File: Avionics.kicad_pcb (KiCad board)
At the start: 4 copper layers, 321.1 x 96.2 mm, 81 parts, among them J1 54-00175, U1 OEM719, U2 TCAN1051VDRBRQ1, U3 INA260AIPWR, U4 TCAN1051VDRBRQ1, U5 INA260AIPWR, U6 TPS543320RPYR

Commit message: OBC: Continue PCB lauout
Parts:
- removed the C3 at (85.9, 65.8)
- removed the C4 at (87.9, 65.8)
- removed the C5 at (83.6, 58.2)
- removed the C6 at (83.6, 60.2)
- removed H1 (x2), H2 (x2): Conn_02x26_Odd_Even, VST104_footprints:ESQ-126-39-x-D
- removed the JP1 at (77.2, 69.9)
- removed the JP2 at (73.8, 69.9)
- removed JP3, JP4: ~, Jumper:SolderJumper-2_P1.3mm_Open_RoundedPad1.0x1.5mm
- removed the MH1 at (181.9, 40.2)
- removed the MH1 at (296.7, 39.9)
- removed the MH2 at (370.3, 39.9)
- removed the MH2 at (255.5, 40.2)
- removed the MH3 at (372.9, 125.7)
- removed the MH3 at (258.1, 125.9)
- removed the MH4 at (292.9, 125.7)
- removed the MH4 at (178.1, 125.9)
- removed the U2 at (87.2, 61.1)
- removed the U4 at (75.4, 75.3)
- added H1COMM1: Conn_02x26_Odd_Even, ESQ-126-39-G-D:SAMTEC_ESQ-126-39-G-D, F.Cu at (186.9, 47.9)
- added H1EPS1: Conn_02x26_Odd_Even, ESQ-126-39-G-D:SAMTEC_ESQ-126-39-G-D, F.Cu at (301.4, 43.1)
- added H2COMM1: Conn_02x26_Odd_Even, ESQ-126-39-G-D:SAMTEC_ESQ-126-39-G-D, F.Cu at (186.9, 42.8)
- added H2EPS1: Conn_02x26_Odd_Even, ESQ-126-39-G-D:SAMTEC_ESQ-126-39-G-D, F.Cu at (301.4, 48.2)
- added J1: SQT-110-01-L-D, SQT-110-01-L-D:SAMTEC_SQT-110-01-L-D, F.Cu at (113.3, 52.1)
- added R7: 1k, Resistor_SMD:R_0805_2012Metric, B.Cu at (62.9, 110.2)
- added R8: 1k, Resistor_SMD:R_0805_2012Metric, B.Cu at (62.9, 113.5)
- added U3: TCAN1046AVDYYRQ1, TCAN1046AV:SOT23_DYY_TEX, B.Cu at (78.1, 64.5)
- H1OBC1: renamed from H1; footprint VST104_footprints:ESQ-126-39-x-D -> ESQ-126-39-G-D:SAMTEC_ESQ-126-39-G-D
- H2OBC1: renamed from H2; footprint VST104_footprints:ESQ-126-39-x-D -> ESQ-126-39-G-D:SAMTEC_ESQ-126-39-G-D
- moved MH5 270.7 mm to (181.9, 40.2)
- moved MH8 249.3 mm to (178.1, 126.0)
- moved MH6 220.4 mm to (255.5, 40.2)
- moved MH9 189.6 mm to (296.3, 40.6)
- moved MH10 178.6 mm to (370.0, 40.6)
- moved MH7 169.8 mm to (258.1, 126.0)
- moved MH12 153.0 mm to (292.5, 126.3)
- moved MH11 90.8 mm to (372.5, 126.3)
- moved C8 51.1 mm to (127.6, 69.0), turned to 180 degrees
- moved U4 50.9 mm to (122.3, 70.9)
- moved R13 18.5 mm to (120.7, 83.6)
- moved C10 18.5 mm to (127.3, 85.3)
- moved C11 18.5 mm to (129.3, 85.3)
- moved C15 18.5 mm to (118.8, 81.0)
- moved C16 18.5 mm to (109.6, 88.6)
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- renumbered C14 to C10, C15 to C11, C16 to C12, C17 to C13, C18 to C14, C19 to C15, C20 to C16, C21 to C17, C22 to C18, C7 to C3, C8 to C4, C9 to C5, C10 to C6, C11 to C7, C12 to C8, C13 to C9, J1 to J2, JP5 to JP1, JP6 to JP2, R8 to R10, R9 to R11, R10 to R12, R11 to R13, R12 to R14, R13 to R15, R14 to R16, R15 to R17, R7 to R9, U3 to U2, U5 to U4, U6 to U5
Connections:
- C16 pad 1: /OBC/TPS543320/VOUT -> /OBC/+5V_OEM719B
- C17 pad 1: /OBC/TPS543320/VOUT -> /OBC/+5V_OEM719B
- C18 pad 1: /OBC/TPS543320/VOUT -> /OBC/+5V_OEM719B
- C4 pad 1: +5V_CM4 -> +3V3
- C5 pad 1: +5V_CM4 -> +3V3
- C6 pad 1: +3V3 -> +5V_CM4
- C7 pad 1: +3V3 -> +5V_CM4
- J2 pad 2: Net-(U1-RXD1) -> /OBC/GNSS_RXD1
- J2 pad 3: Net-(U1-TXD1) -> /OBC/GNSS_TXD1
- JP1 pad 2: Net-(JP5-B) -> Net-(JP1-B)
- JP2 pad 1: Net-(JP6-A) -> Net-(JP2-A)
- L1 pad 2: /OBC/TPS543320/VOUT -> /OBC/+5V_OEM719B
- Module1 pad 34: /OBC/GNSS_RXD -> /OBC/GNSS_RXD2
- Module1 pad 54: /OBC/GNSS_TXD -> /OBC/GNSS_TXD2
- Module1 pad 89: Net-(JP5-B) -> Net-(Module1A-WiFi_nDisable)
- Module1 pad 91: Net-(JP6-A) -> Net-(Module1A-BT_nDisable)
- Module1 pad SH1: GND -> (no net)
- Module1 pad SH2: GND -> (no net)
- Module1 pad SH3: GND -> (no net)
- Module1 pad SH4: GND -> (no net)
- R1 pad 1: Net-(JP1-A) -> /OBC/CAN_A_H
- R17 pad 2: /OBC/TPS543320/VOUT -> /OBC/+5V_OEM719B
- R2 pad 2: Net-(JP2-B) -> /OBC/CAN_A_L
- R3 pad 1: Net-(JP3-A) -> /OBC/CAN_B_H
- R4 pad 2: Net-(JP4-B) -> /OBC/CAN_B_L
- U1 pad 1: GND -> unconnected-(U1-NC-Pad1)
- U1 pad 2: GND -> /OBC/+5V_OEM719B
- U1 pad 3: GND -> unconnected-(U1-USB_D--Pad3)
- U1 pad 4: GND -> unconnected-(U1-USB_D+/RXD3-Pad4)
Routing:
- net /OBC/SDA0: track 2.86 -> 102.4 mm, vias 1 -> 3
- net /OBC/SCL0: track 2.84 -> 100.6 mm, vias 1 -> 3
- net /OBC/UART_DATA_RX: track 0.00 -> 85.1 mm
- net /OBC/UART_DATA_TX: track 0.00 -> 82.2 mm, vias 0 -> 4
- net /OBC/GNSS_TXD1: track 0.00 -> 77.2 mm
- net /OBC/GNSS_PPS: track 0.00 -> 71.6 mm, vias 0 -> 1
- net /OBC/UART_COMM_TX: track 0.00 -> 65.9 mm, vias 0 -> 2
- net /OBC/UART_COMM_RX: track 0.00 -> 64.3 mm
- net /OBC/GNSS_RXD1: track 0.00 -> 62.5 mm, vias 0 -> 1
- net +3V3: track 16.8 -> 67.6 mm
- net +5V_GNSS: track 7.04 -> 54.2 mm, vias 1 -> 0
- net /OBC/PI_nLED_Activity: track 0.00 -> 46.6 mm, vias 0 -> 2
- net /OBC/CAN_B_S: track 0.00 -> 44.1 mm, vias 0 -> 2
- net /OBC/CAN_A_TXD: track 0.00 -> 43.7 mm, vias 0 -> 2
- net /OBC/CAN_A_S: track 0.00 -> 43.7 mm, vias 0 -> 2
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- added copper zone on B.Cu, net +5V_CM4
- added copper zone on B.Cu, net +5V_MPU
- added copper zone on B.Cu, net /OBC/+5V_OEM719B
- added copper zone on F.Cu, net /OBC/+5V_OEM719B
- added copper zone on In1.Cu, net /OBC/+5V_OEM719B
- removed copper zone on In1.Cu, net +5V_GNSS
- removed copper zone on B.Cu, net /OBC/TPS543320/VOUT
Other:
- board size 321.1 x 96.2 mm -> 320.9 x 96.5 mm

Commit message: Continue PCB layout
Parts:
- removed J2: 54-00175, 54_00175-audio-jack:TENSILITY_54-00175
- moved R10 72.3 mm to (127.8, 67.4), turned to 180 degrees
- moved R9 67.2 mm to (123.9, 67.4), turned to 0 degrees
- moved R8 49.8 mm to (100.0, 80.3), turned to 90 degrees
- moved JP2 49.3 mm to (99.8, 76.8), turned to 90 degrees
- moved JP1 49.3 mm to (102.4, 76.8), turned to -90 degrees
- moved R7 49.3 mm to (102.1, 80.3), turned to -90 degrees
- moved U4 9.08 mm to (125.9, 62.6)
- moved C8 7.89 mm to (130.4, 61.7), turned to 90 degrees
- moved Module1 0.55 mm to (78.8, 93.5), turned to -90 degrees
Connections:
- C16 pad 1: /OBC/+5V_OEM719B -> +5V_OEM719B
- C17 pad 1: /OBC/+5V_OEM719B -> +5V_OEM719B
- C18 pad 1: /OBC/+5V_OEM719B -> +5V_OEM719B
- H1OBC1 pad 42: /OBC/UART_F_TX -> /OBC/GNSS_TXD1
- H1OBC1 pad 44: /OBC/UART_F_RX -> /OBC/GNSS_RXD1
- J1 pad 02: /OBC/+5V_OEM719B -> +5V_OEM719B
- L1 pad 2: /OBC/+5V_OEM719B -> +5V_OEM719B
- R17 pad 2: /OBC/+5V_OEM719B -> +5V_OEM719B
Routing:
- net /OBC/GNSS_TXD1: track 77.2 -> 7.82 mm
- net /OBC/GNSS_NRESET_IN: track 0.00 -> 68.7 mm, vias 0 -> 2
- net /OBC/GNSS_RXD2: track 0.00 -> 68.0 mm
- net /OBC/GNSS_PV: track 0.00 -> 61.3 mm
- net /OBC/GNSS_TXD2: track 0.00 -> 58.8 mm, vias 0 -> 2
- net /OBC/GNSS_RXD1: track 62.5 -> 10.4 mm, vias 1 -> 0
- net +3V3: track 67.6 -> 16.6 mm, vias 2 -> 3
- net /OBC/nPWR_LED: track 26.8 -> 67.5 mm, vias 0 -> 2
- net +5V_OEM719B: track 0.00 -> 31.8 mm
- net /OBC/SCL0: track 100.6 -> 75.2 mm
- net /OBC/SDA0: track 102.4 -> 81.3 mm
- net /OBC/UART_DATA_TX: track 82.2 -> 63.0 mm, vias 4 -> 2
- net /OBC/UART_DATA_RX: track 85.1 -> 67.4 mm, vias 0 -> 2
- net /OBC/UART_COMM_RX: track 64.3 -> 52.2 mm, vias 0 -> 1
- net /OBC/CAN_B_RXD: track 36.2 -> 47.9 mm
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- added copper zone on In1.Cu, net +3V3
- added copper zone on B.Cu, net +5V_OEM719B
- removed copper zone on B.Cu, net /OBC/+5V_OEM719B
- removed copper zone on F.Cu, net /OBC/+5V_OEM719B
- removed copper zone on In1.Cu, net /OBC/+5V_OEM719B

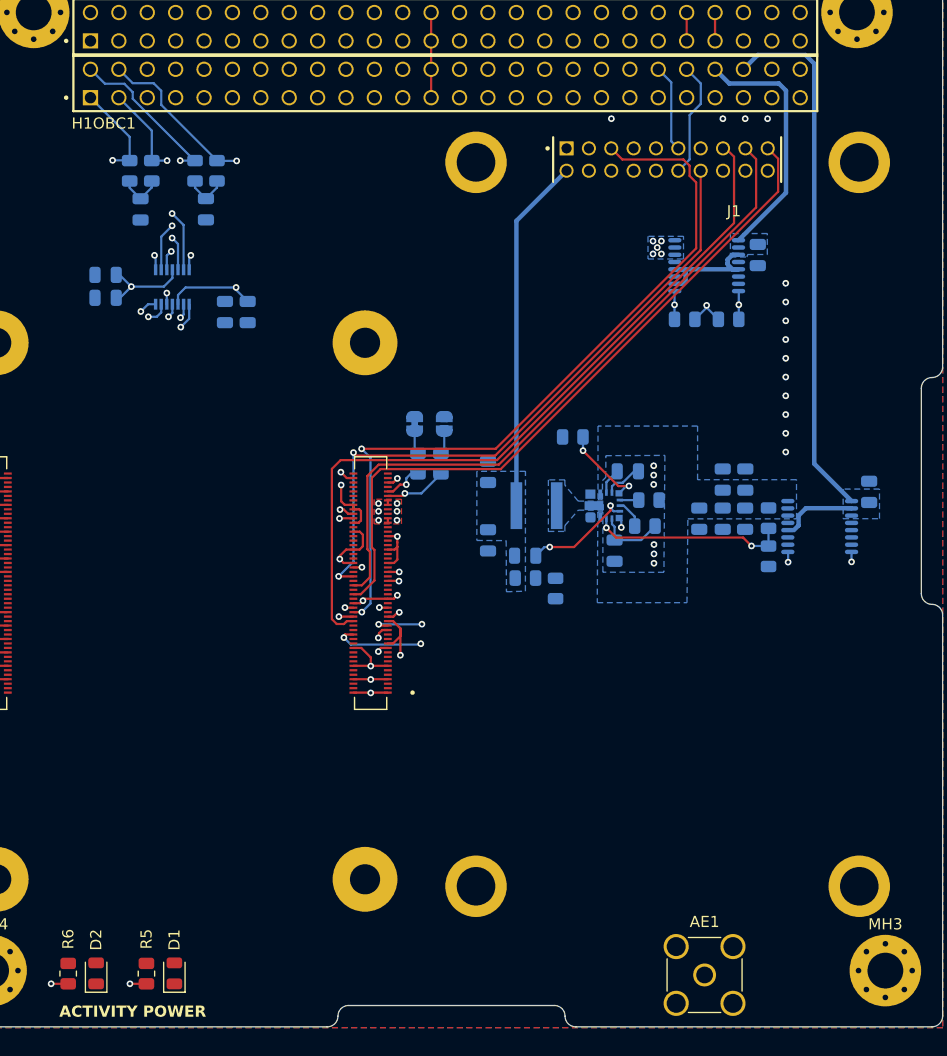
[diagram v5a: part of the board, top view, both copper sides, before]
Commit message: OBC: complete layout first pass
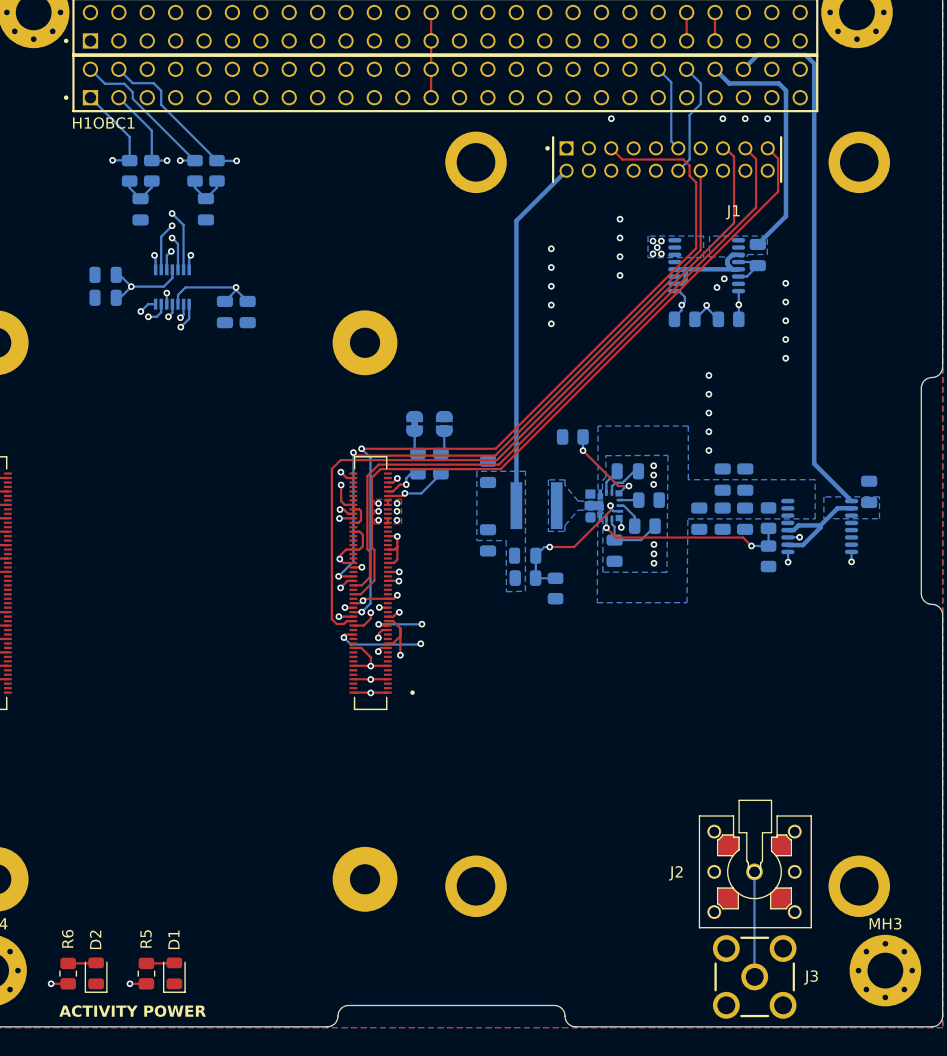
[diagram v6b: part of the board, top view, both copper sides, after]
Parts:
- removed AE1: Antenna, Connector_Coaxial:SMA_Amphenol_901-144_Vertical
- added J2: MMBX-S50-0-18, Novatel:MMBX-S50-0-18, F.Cu at (130.2, 116.8)
- added J3: SMA-J-P-X-RA-TH1, SMA_J_P_H_RA_TH1:SAMTEC_SMA-J-P-X-RA-TH1, F.Cu at (130.2, 126.3)
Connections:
- Module1 pad 88: Net-(Module1A-+1.8v_(Output)-Pad88) -> unconnected-(Module1A-+1.8v_(Output)-Pad88)
- Module1 pad 90: Net-(Module1A-+1.8v_(Output)-Pad88) -> unconnected-(Module1A-+1.8v_(Output)-Pad90)
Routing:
- net /OBC/RF_GNSS: track 0.00 -> 9.41 mm
- net GND: track 84.1 -> 92.9 mm, vias 48 -> 62
- net Net-(U5-FB): track 9.97 -> 13.8 mm
- net +5V_GNSS: track 54.2 -> 58.0 mm
- net Net-(D2-A): track 0.00 -> 2.52 mm
- net Net-(D1-A): track 0.00 -> 2.52 mm
- net +3V3: track 16.6 -> 18.2 mm
- net /OBC/SCL0: track 75.2 -> 75.9 mm

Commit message: Layout confirmed, PCBs ordered
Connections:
- H1OBC1 pad 29: GND -> unconnected-(H1OBC1-Pad29)
- H1OBC1 pad 30: GND -> unconnected-(H1OBC1-Pad30)
- H1OBC1 pad 31: GND -> /OBC/CHARGE
- H1OBC1 pad 32: GND -> /OBC/CHARGE
- H1OBC1 pad 33: unconnected-(H1OBC1-Pad33) -> GND
- H1OBC1 pad 34: unconnected-(H1OBC1-Pad34) -> GND
- H2OBC1 pad 43: /OBC/CHARGE -> unconnected-(H2OBC1-Pad43)
- H2OBC1 pad 44: /OBC/CHARGE -> unconnected-(H2OBC1-Pad44)
- H2OBC1 pad 47: /OBC/RBF_A -> /OBC/RBF_C
- H2OBC1 pad 48: /OBC/DS_A -> /OBC/DS_C
- H2OBC1 pad 49: /OBC/RBF_B -> /OBC/RBF_A
- H2OBC1 pad 50: /OBC/DS_B -> /OBC/RBF_B
- H2OBC1 pad 51: /OBC/RBF_C -> /OBC/DS_A
- H2OBC1 pad 52: /OBC/DS_C -> /OBC/DS_B
